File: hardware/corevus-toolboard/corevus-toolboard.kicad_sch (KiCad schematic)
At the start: 87 parts, among them J1 MF3 1x2P, J10 1x3P, J2 XH 1x2P, J3 MX3.0 2x4P, J4 XH 1x4P, J5 XH 1x2P, J6 XH 1x2P, J7 XH 1x2P, J8 1x8P, J9 XH 1x2P, Q2 NMOS, Q4 AO3400, SW3 Reset, U1 LIS2DE12, U2 TPS54302, U3 STM32G431KBU3, U4 TMC2209-LA, U6 SPX3819M5-L-3-3, U7 TPS2069CDBV, U8 UCC27517, Y1 XRCGB25

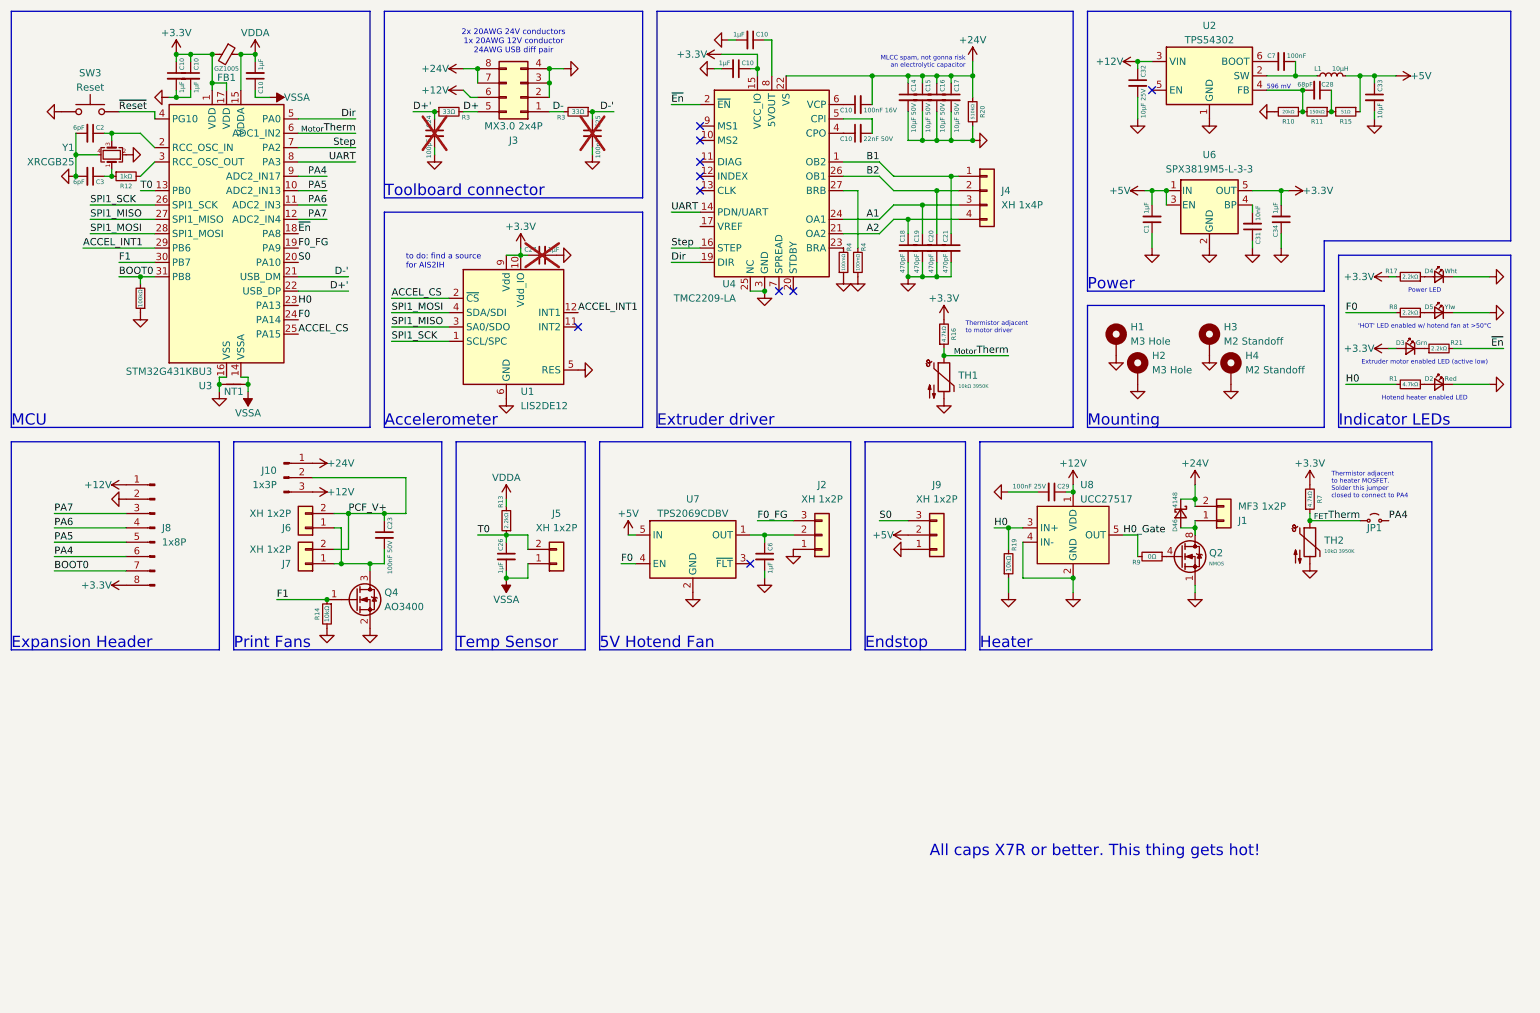
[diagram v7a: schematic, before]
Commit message: Added STEP and Parasolid mechanical files for Corevus-G v0.6, added TMC2160 + Heater module, added toolboard 4x thermistor expansion, added toolboard MAX31856 thermocouple ADC expansion
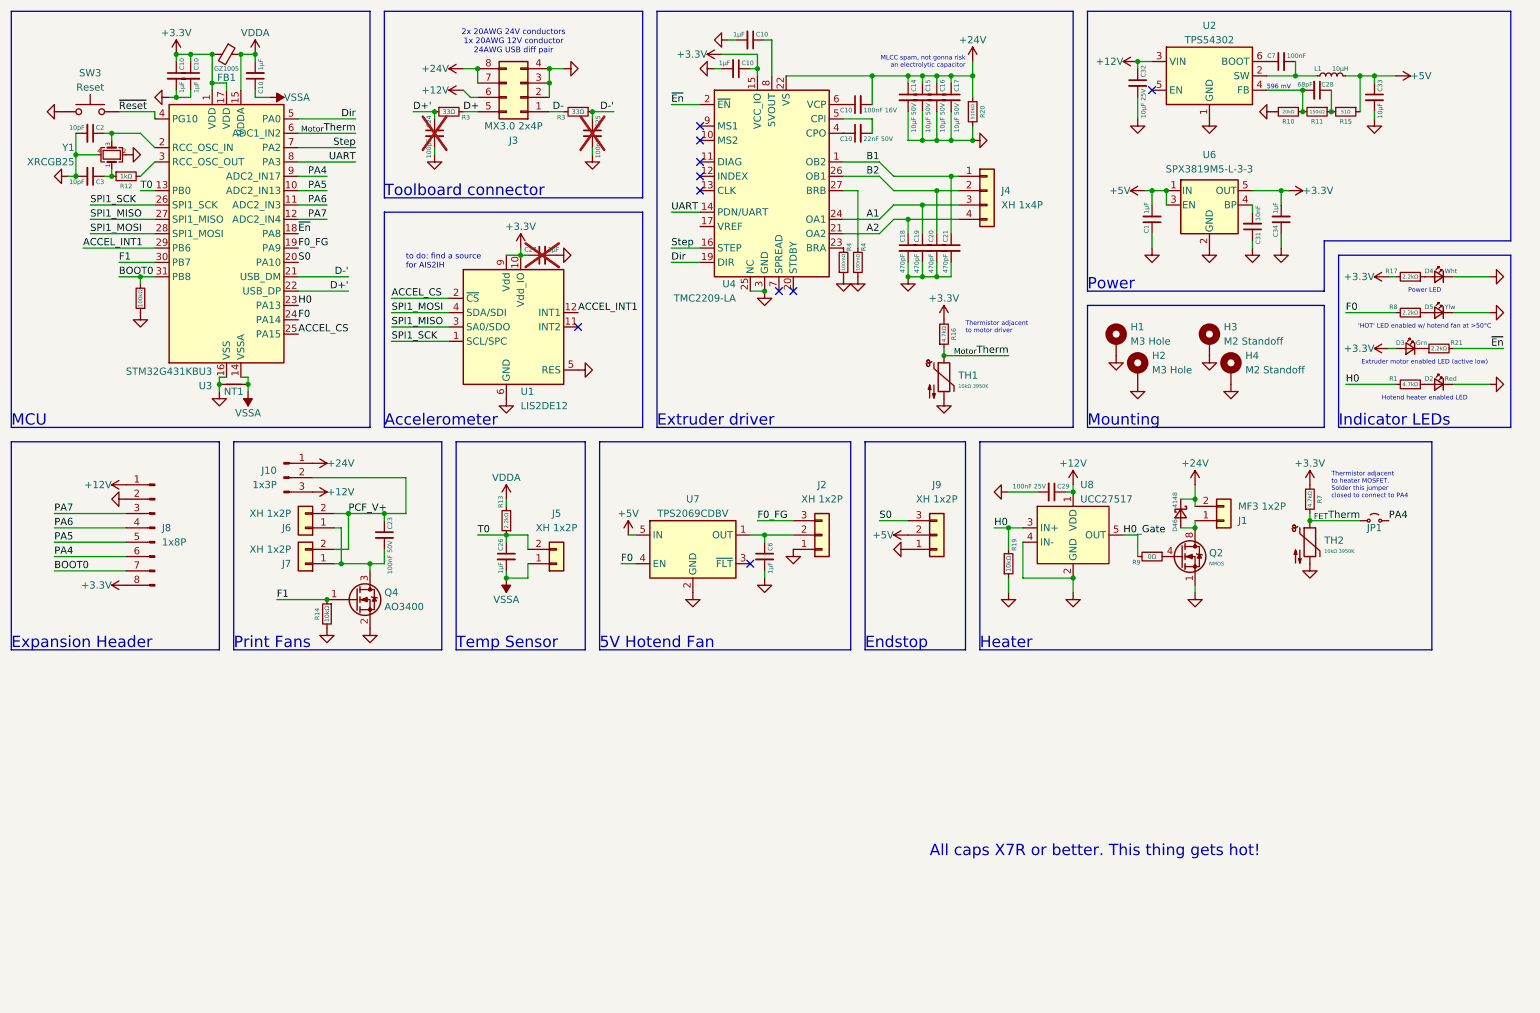
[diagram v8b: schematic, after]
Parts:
- C2, C3: value 6pF -> 10pF
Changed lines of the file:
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@@
 	(wire
 		(pts
-			(xy 224.79 107.95) (xy 224.79 106.68)
-		)
-		(stroke
-			(width 0)
-			(type default)
-		)
-	)
-	(wire
-		(pts
 			(xy 71.12 49.53) (xy 66.04 49.53)
 		)
@@
 		)
 	)
+	(wire
+		(pts
+			(xy 25.4 44.45) (xy 26.67 44.45)
+		)
+		(stroke
+			(width 0)
+			(type default)
+		)
+	)
 	(polyline
 		(pts
@@
 			)
 		)
-		(property "Value" "6pF"
+		(property "Value" "10pF"
 			(at 28.21 35.83 90)
 			(effects
@@
 	(symbol
 		(lib_id "power:GND")
-		(at 26.67 44.45 270)
+		(at 25.4 44.45 270)
 		(mirror x)
 		(unit 1)
@@
 		(dnp no)
 		(property "Reference" "#PWR038"
-			(at 20.32 44.45 0)
+			(at 19.05 44.45 0)
 			(effects
 				(font
@@
 		)
 		(property "Value" "GND"
-			(at 24.13 44.45 90)
+			(at 22.86 44.45 90)
 			(effects
 				(font
@@
 		)
 		(property "Footprint" ""
-			(at 26.67 44.45 0)
+			(at 25.4 44.45 0)
 			(effects
 				(font
@@
 		)
 		(property "Datasheet" ""
-			(at 26.67 44.45 0)
+			(at 25.4 44.45 0)
 			(effects
 				(font
@@
 		)
 		(property "Description" ""
-			(at 26.67 44.45 0)
+			(at 25.4 44.45 0)
 			(effects
 				(font
@@
 			)
 		)
-		(property "Value" "6pF"
+		(property "Value" "10pF"
 			(at 28.21 45.45 90)
 			(effects
